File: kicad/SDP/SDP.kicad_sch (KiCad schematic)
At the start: 72 parts

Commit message: Added footprints
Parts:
- C1: footprint (none) -> Capacitor_SMD:C_0805_2012Metric
- C10, C11, C12, C15, C16, C17, C18, C20, C21, C22, C23, C24, C25, C26, C27, C9: renamed from C?; footprint (none) -> Capacitor_SMD:C_0805_2012Metric
- C2, C3, C4, C5, C6: footprint (none) -> Capacitor_SMD:C_0603_1608Metric
- C7: renamed from C?; footprint (none) -> Capacitor_SMD:C_0603_1608Metric
- C8: renamed from C?; footprint (none) -> Capacitor_SMD:C_1206_3216Metric
- gave numbers to parts that had none: 46

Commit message: Added footprints
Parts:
- BT1: footprint (none) -> Keystone_1056:1056
- C14: footprint (none) -> Capacitor_SMD:C_1206_3216Metric
- D1, D5: footprint (none) -> LED_SMD:LED_0805_2012Metric
- D3, D4: value B230A -> CDBA240-G; footprint (none) -> Diode_SMD:D_SMA
- F1: footprint (none) -> Fuse:Fuse_1206_3216Metric
- L1: footprint (none) -> DR125-220-R:DR125-220-R
- R1, R10, R11, R12, R13, R14, R15, R16, R17, R18, R2, R3, R5, R6, R7, R8, R9: footprint (none) -> Resistor_SMD:R_0805_2012Metric
- R19: value 2k -> 2k2; footprint (none) -> Resistor_SMD:R_0805_2012Metric
- R4: value 1k -> 10k; footprint (none) -> Resistor_SMD:R_0805_2012Metric
- Y1: footprint (none) -> ECS-80-20-5PXDU-TR:XTAL_ECS-80-20-5PXDU-TR
- Y2: footprint (none) -> CFS206:CFS206-32.768-KDZF-UB

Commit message: Assigned footprints, added limit switches, rearranged schematics
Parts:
- C13: footprint (none) -> EEETG1C331UP:EEETG1C331UP
- C19: footprint (none) -> EEVTG1C471Q:EEVTG1C471Q
- D2: value 12V -> 1SMA5927BT3G; footprint (none) -> Diode_SMD:D_SMA
- J1: footprint (none) -> Connector_PinSocket_2.54mm:PinSocket_2x12_P2.54mm_Vertical
- J2, J3: footprint (none) -> Connector_PinSocket_2.54mm:PinSocket_2x04_P2.54mm_Vertical
- J4: footprint (none) -> Connector_PinSocket_2.54mm:PinSocket_2x02_P2.54mm_Vertical
- J5, J6: footprint (none) -> Connector_PinSocket_2.54mm:PinSocket_1x04_P2.54mm_Vertical
- J7: footprint (none) -> 50TZV100M:50TZV100M8X10.5
- MOSFET1: footprint SOT-23F_TOS -> Package_TO_SOT_SMD:SOT-23
- U3: footprint TQFP100_12x12MC_MCH -> PIC24FJ128GA010-I-PT:PIC24FJ128GA010-I&slash_PT
- U4: footprint 21-0042B_16_MXM -> DS3231SN:DS3231SN-T&R
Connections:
- net P72_FAN: now reaches U3.72 (OC1/RD0)
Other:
- removed sheet BrewingSubsystem
- removed sheet FilterSubsystem
- removed sheet GrinderSubsystem
- added sheet Sensors (sensors.kicad_sch)
- added sheet StepperMotors (steppermotors.kicad_sch)
- moved on the sheet: J1, J2, J3, J4

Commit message: Assigned footprints and removed ferrite bead
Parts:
- removed FB1: FerriteBead_Small, symbol Device:FerriteBead_Small
- added C37, C38: 10u, Capacitor_SMD:C_1206_3216Metric, symbol Device:C_Small
- L2: footprint (none) -> Inductor_SMD:L_12x12mm_H8mm
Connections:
- net +12V: now also D2.1 (K), MOSFET1.2 (SOURCE), C37.1, C38.1
- net GND: now also U1.7 (GND), U2.7 (GND), C37.2, C38.2
- no-connect marks 1 -> 10

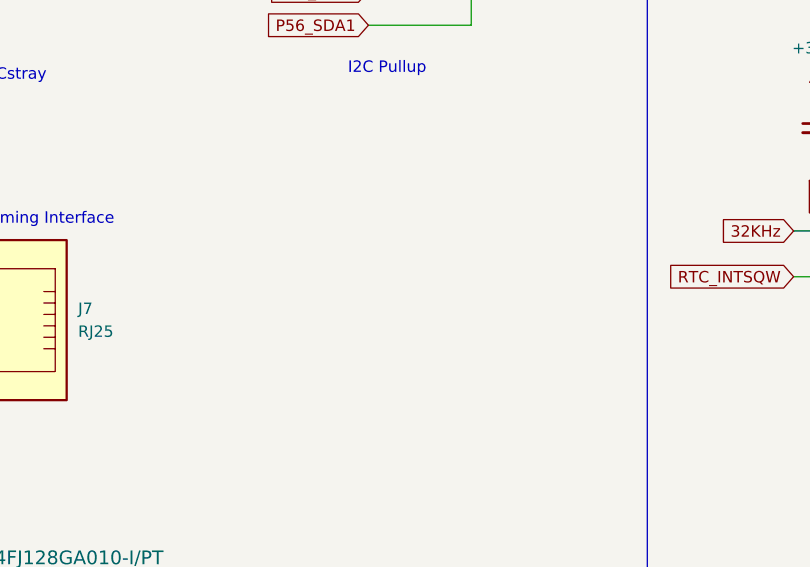
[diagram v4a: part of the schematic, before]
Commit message: Added MCLR pullup and assigned footprints
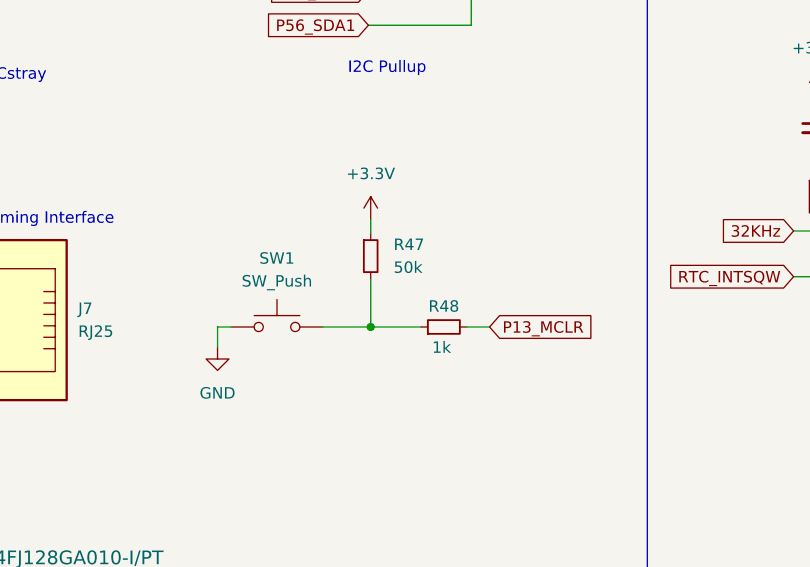
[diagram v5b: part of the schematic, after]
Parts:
- added R47: 50k, Resistor_SMD:R_0805_2012Metric, symbol Device:R_Small
- added R48: 1k, Resistor_SMD:R_0805_2012Metric, symbol Device:R_Small
- added SW1: SW_Push, 1825910-6:SW_1825910-6-4, symbol Switch:SW_Push
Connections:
- net +3V3: now also R47.1
- net GND: now also SW1.1
- net P13_MCLR: now also R48.2
- new net: R47.2, R48.1, SW1.2
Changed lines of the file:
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@@
   (junction (at 56.134 85.344) (diameter 0) (color 0 0 0 0)
   )
+  (junction (at 269.24 214.884) (diameter 0) (color 0 0 0 0)
+  )
   (junction (at 147.32 79.756) (diameter 0) (color 0 0 0 0)
   )
@@
     (stroke (width 0) (type default) (color 0 0 0 0))
   )
+  (wire (pts (xy 263.906 214.884) (xy 269.24 214.884))
+    (stroke (width 0) (type default) (color 0 0 0 0))
+  )
   (wire (pts (xy 307.086 21.59) (xy 308.356 21.59))
     (stroke (width 0) (type default) (color 0 0 0 0))
@@
     (stroke (width 0) (type default) (color 0 0 0 0))
   )
+  (wire (pts (xy 253.746 214.884) (xy 252.222 214.884))
+    (stroke (width 0) (type default) (color 0 0 0 0))
+  )
   (wire (pts (xy 134.112 44.958) (xy 134.112 56.896))
     (stroke (width 0) (type default) (color 0 0 0 0))
@@
     (stroke (width 0) (type default) (color 0 0 0 0))
   )
+  (wire (pts (xy 269.24 214.884) (xy 274.828 214.884))
+    (stroke (width 0) (type default) (color 0 0 0 0))
+  )
   (wire (pts (xy 278.892 243.078) (xy 278.892 245.872))
     (stroke (width 0) (type default) (color 0 0 0 0))
@@
     (stroke (width 0) (type default) (color 0 0 0 0))
   )
+  (wire (pts (xy 269.24 209.55) (xy 269.24 214.884))
+    (stroke (width 0) (type default) (color 0 0 0 0))
+  )
   (wire (pts (xy 213.868 217.932) (xy 217.678 217.932))
     (stroke (width 0) (type default) (color 0 0 0 0))
@@
     (stroke (width 0) (type default) (color 0 0 0 0))
   )
+  (wire (pts (xy 279.908 214.884) (xy 282.448 214.884))
+    (stroke (width 0) (type default) (color 0 0 0 0))
+  )
+  (wire (pts (xy 252.222 214.884) (xy 252.222 217.17))
+    (stroke (width 0) (type default) (color 0 0 0 0))
+  )
   (wire (pts (xy 318.77 195.326) (xy 318.77 196.596))
     (stroke (width 0) (type default) (color 0 0 0 0))
@@
     (stroke (width 0) (type default) (color 0 0 0 0))
   )
+  (wire (pts (xy 269.24 202.946) (xy 269.24 204.47))
+    (stroke (width 0) (type default) (color 0 0 0 0))
+  )
   (wire (pts (xy 40.64 201.93) (xy 41.91 201.93))
     (stroke (width 0) (type default) (color 0 0 0 0))
@@
     )
   )
+  (global_label "P13_MCLR" (shape input) (at 282.448 214.884 0) (fields_autoplaced)
+    (effects (font (size 1.27 1.27)) (justify left))
+    (property "Intersheet References" "${INTERSHEET_REFS}" (id 0) (at 294.5373 214.9634 0)
+      (effects (font (size 1.27 1.27)) (justify left) hide)
+    )
+  )
   (global_label "P99_RE3" (shape input) (at 322.326 34.29 0) (fields_autoplaced)
     (effects (font (size 1.27 1.27)) (justify left))
@@
     (pin "75")
   )
+  (symbol (lib_id "Device:R_Small") (at 269.24 207.01 0) (unit 1)
+    (in_bom yes) (on_board yes) (fields_autoplaced)
+    (property "Reference" "R47" (id 0) (at 271.78 205.7399 0)
+      (effects (font (size 1.27 1.27)) (justify left))
+    )
+    (property "Value" "50k" (id 1) (at 271.78 208.2799 0)
+      (effects (font (size 1.27 1.27)) (justify left))
+    )
+    (property "Footprint" "Resistor_SMD:R_0805_2012Metric" (id 2) (at 269.24 207.01 0)
+      (effects (font (size 1.27 1.27)) hide)
+    )
+    (property "Datasheet" "~" (id 3) (at 269.24 207.01 0)
+      (effects (font (size 1.27 1.27)) hide)
+    )
+    (pin "1")
+    (pin "2")
+  )
   (symbol (lib_name "GND_2") (lib_id "power:GND") (at 334.01 228.346 0) (unit 1)
     (in_bom yes) (on_board yes) (fields_autoplaced)
@@
     (pin "2")
   )
+  (symbol (lib_id "Device:R_Small") (at 277.368 214.884 90) (unit 1)
+    (in_bom yes) (on_board yes)
+    (property "Reference" "R48" (id 0) (at 277.368 212.598 90))
+    (property "Value" "1k" (id 1) (at 277.114 217.17 90))
+    (property "Footprint" "Resistor_SMD:R_0805_2012Metric" (id 2) (at 277.368 214.884 0)
+      (effects (font (size 1.27 1.27)) hide)
+    )
+    (property "Datasheet" "~" (id 3) (at 277.368 214.884 0)
+      (effects (font (size 1.27 1.27)) hide)
+    )
+    (pin "1")
+    (pin "2")
+  )
+  (symbol (lib_name "GND_2") (lib_id "power:GND") (at 252.222 217.17 0) (unit 1)
+    (in_bom yes) (on_board yes) (fields_autoplaced)
+    (property "Reference" "#PWR0233" (id 0) (at 252.222 223.52 0)
+      (effects (font (size 1.27 1.27)) hide)
+    )
+    (property "Value" "GND" (id 1) (at 252.222 222.25 0))
+    (property "Footprint" "" (id 2) (at 252.222 217.17 0)
+      (effects (font (size 1.27 1.27)) hide)
+    )
+    (property "Datasheet" "" (id 3) (at 252.222 217.17 0)
+      (effects (font (size 1.27 1.27)) hide)
+    )
+    (pin "1")
+  )
   (symbol (lib_id "Device:R_Small") (at 160.782 92.456 0) (unit 1)
     (in_bom yes) (on_board yes) (fields_autoplaced)
@@
     (pin "1")
   )
+  (symbol (lib_id "Switch:SW_Push") (at 258.826 214.884 0) (unit 1)
+    (in_bom yes) (on_board yes) (fields_autoplaced)
+    (property "Reference" "SW1" (id 0) (at 258.826 207.264 0))
+    (property "Value" "SW_Push" (id 1) (at 258.826 209.804 0))
+    (property "Footprint" "1825910-6:SW_1825910-6-4" (id 2) (at 258.826 209.804 0)
+      (effects (font (size 1.27 1.27)) hide)
+    )
+    (property "Datasheet" "~" (id 3) (at 258.826 209.804 0)
+      (effects (font (size 1.27 1.27)) hide)
+    )
+    (pin "1")
+    (pin "2")
+  )
   (symbol (lib_id "Device:L_Small") (at 261.366 38.1 90) (unit 1)
     (in_bom yes) (on_board yes) (fields_autoplaced)
@@
     (pin "1")
   )
+  (symbol (lib_name "+3.3V_1") (lib_id "power:+3.3V") (at 269.24 202.946 0) (unit 1)
+    (in_bom yes) (on_board yes) (fields_autoplaced)
+    (property "Reference" "#PWR0232" (id 0) (at 269.24 206.756 0)
+      (effects (font (size 1.27 1.27)) hide)
+    )
+    (property "Value" "+3.3V" (id 1) (at 269.24 197.866 0))
+    (property "Footprint" "" (id 2) (at 269.24 202.946 0)
+      (effects (font (size 1.27 1.27)) hide)
+    )
+    (property "Datasheet" "" (id 3) (at 269.24 202.946 0)
+      (effects (font (size 1.27 1.27)) hide)
+    )
+    (pin "1")
+  )
   (symbol (lib_id "Device:C_Small") (at 310.642 157.48 0) (unit 1)
     (in_bom yes) (on_board yes)
@@
       (reference "#PWR0231") (unit 1) (value "GND") (footprint "")
     )
+    (path "/d98d43c9-0502-4869-b844-4eb8f381919d"
+      (reference "#PWR0232") (unit 1) (value "+3.3V") (footprint "")
+    )
+    (path "/7d2737ed-c38b-4b2d-896d-2b65861c9eb6"
+      (reference "#PWR0233") (unit 1) (value "GND") (footprint "")
+    )
     (path "/5cb21baf-fafc-42b6-a9e2-44994cc19a47/67efea03-a238-479f-b70d-2108752c2833"
       (reference "A1") (unit 1) (value "Pololu_Breakout_A4988") (footprint "Module:Pololu_Breakout-16_15.2x20.3mm")
@@
       (reference "R46") (unit 1) (value "10k") (footprint "Resistor_SMD:R_0805_2012Metric")
     )
+    (path "/76647376-e1e0-4042-a4d7-e5a6ee47b95b"
+      (reference "R47") (unit 1) (value "50k") (footprint "Resistor_SMD:R_0805_2012Metric")
+    )
+    (path "/7d01d583-4a6f-4da6-a03f-98181f5e485b"
+      (reference "R48") (unit 1) (value "1k") (footprint "Resistor_SMD:R_0805_2012Metric")
+    )
+    (path "/9c9bfbc5-fb55-43d3-8ad9-7d76c83cd984"
+      (reference "SW1") (unit 1) (value "SW_Push") (footprint "1825910-6:SW_1825910-6-4")
+    )
     (path "/9674121a-8497-4165-869e-8c6606f7fd85"

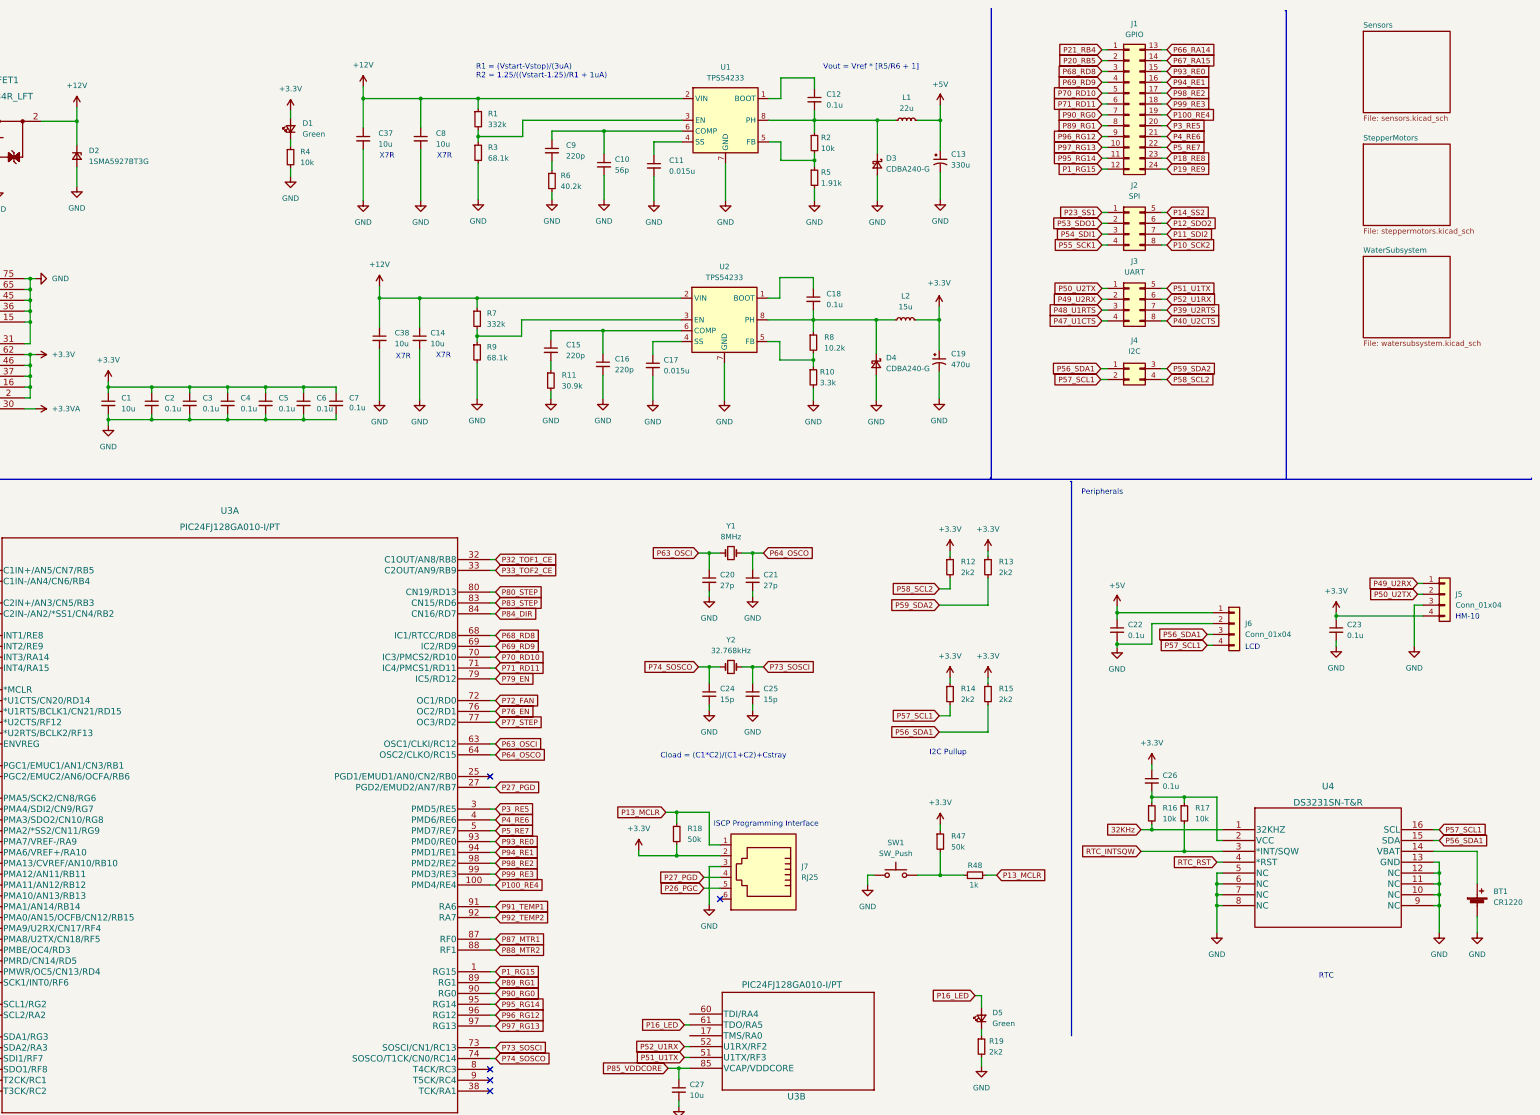
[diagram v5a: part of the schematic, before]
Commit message: Added input filter and power headers
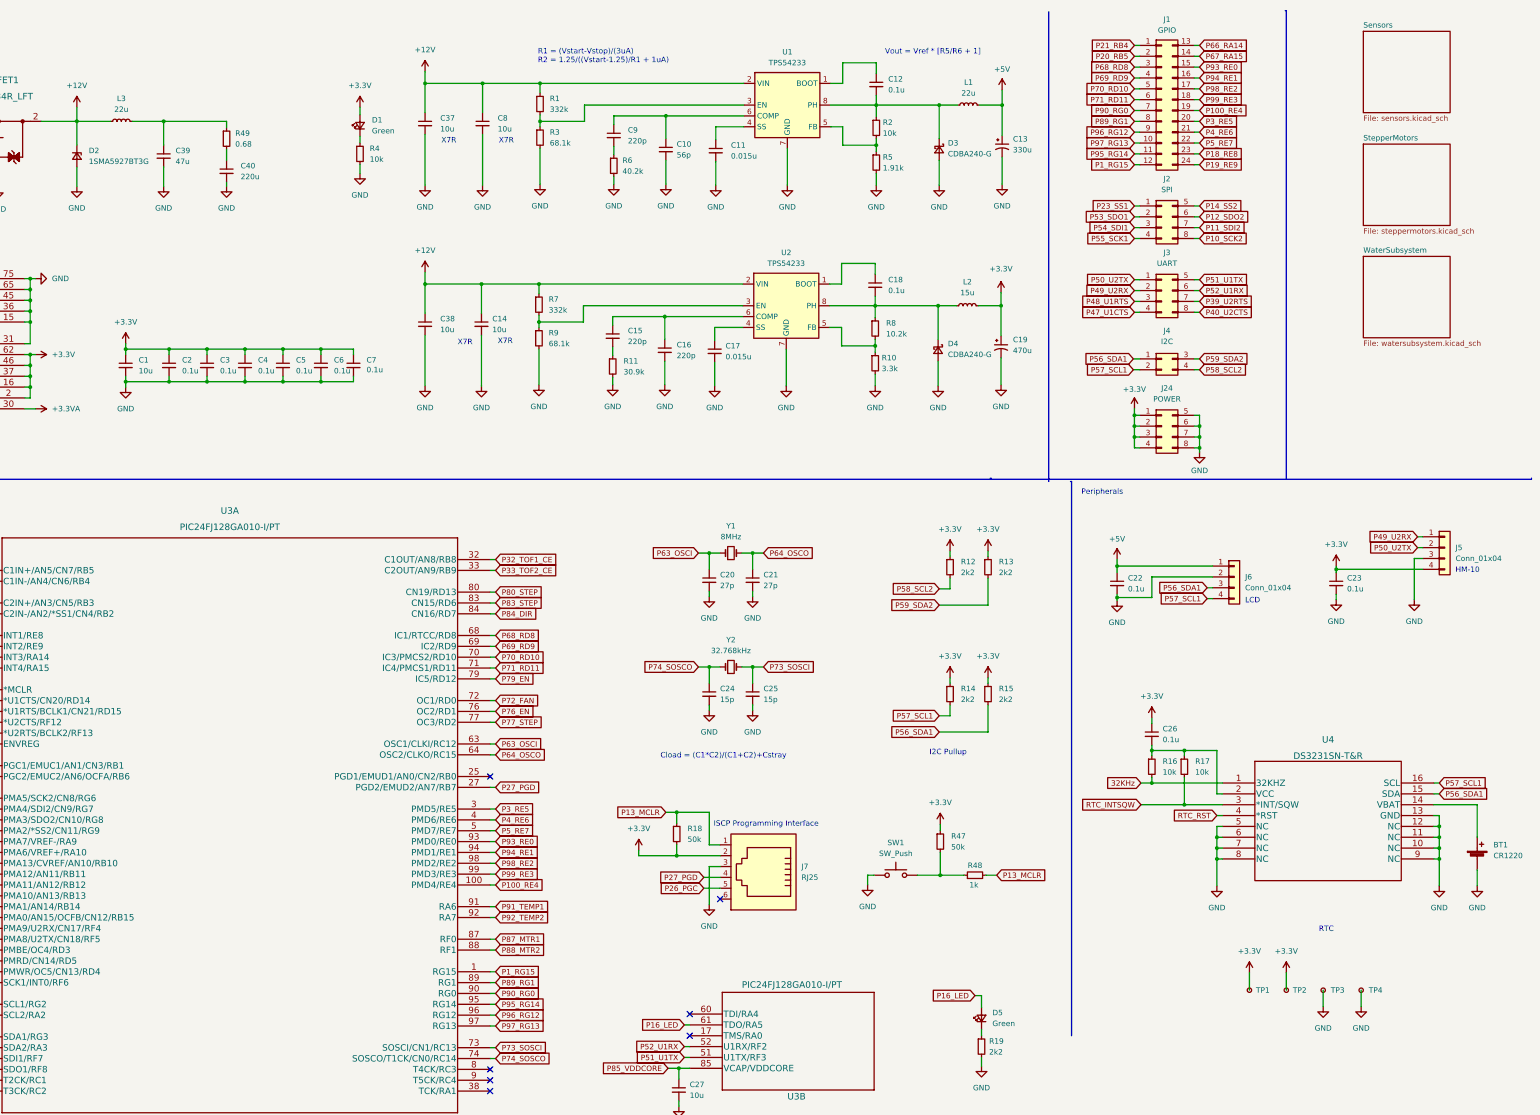
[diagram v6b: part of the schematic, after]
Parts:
- added C39: 47u, Capacitor_THT:C_Radial_D8.0mm_H11.5mm_P3.50mm, symbol Device:C_Small
- added C40: 220u, Capacitor_THT:C_Radial_D10.0mm_H16.0mm_P5.00mm, symbol Device:C_Small
- added J24: POWER, Connector_PinSocket_2.54mm:PinSocket_2x04_P2.54mm_Vertical, symbol Connector_Generic:Conn_02x04_Top_Bottom
- added L3: 22u, DR125-220-R:DR125-220-R, symbol Device:L_Small
- added R49: 0.68, Resistor_SMD:R_0805_2012Metric, symbol Device:R_Small
- added TP1, TP2, TP3, TP4: TestPoint_Small, symbol Connector:TestPoint_Small
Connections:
- net +12V: now also L3.1
- net +3V3: now also J24.1 (Pin_1), J24.2 (Pin_2), J24.3 (Pin_3), J24.4 (Pin_4), TP1.1, TP2.1
- net GND: now also C39.2, C40.2, J24.5 (Pin_5), J24.6 (Pin_6), J24.7 (Pin_7), J24.8 (Pin_8), TP3.1, TP4.1
- new net: C39.1, L3.2, R49.1
- new net: C40.1, R49.2
- no-connect marks 10 -> 12
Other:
- moved on the sheet: BT1, C1, C10, C11, C12, C13, C14, C15, C16, C17, C18, C19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
